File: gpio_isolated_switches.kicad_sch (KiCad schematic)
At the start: 34 parts, among them J2 Conn_01x02, J3 Conn_01x02, J4 Conn_01x02, J5 SBC GPIO, J6 Conn_01x02, J7 Conn_01x02, Q2 BUK7M10-40EX, Q3 BUK7M10-40EX, Q4 BUK7M10-40EX, U1 TLP291-4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

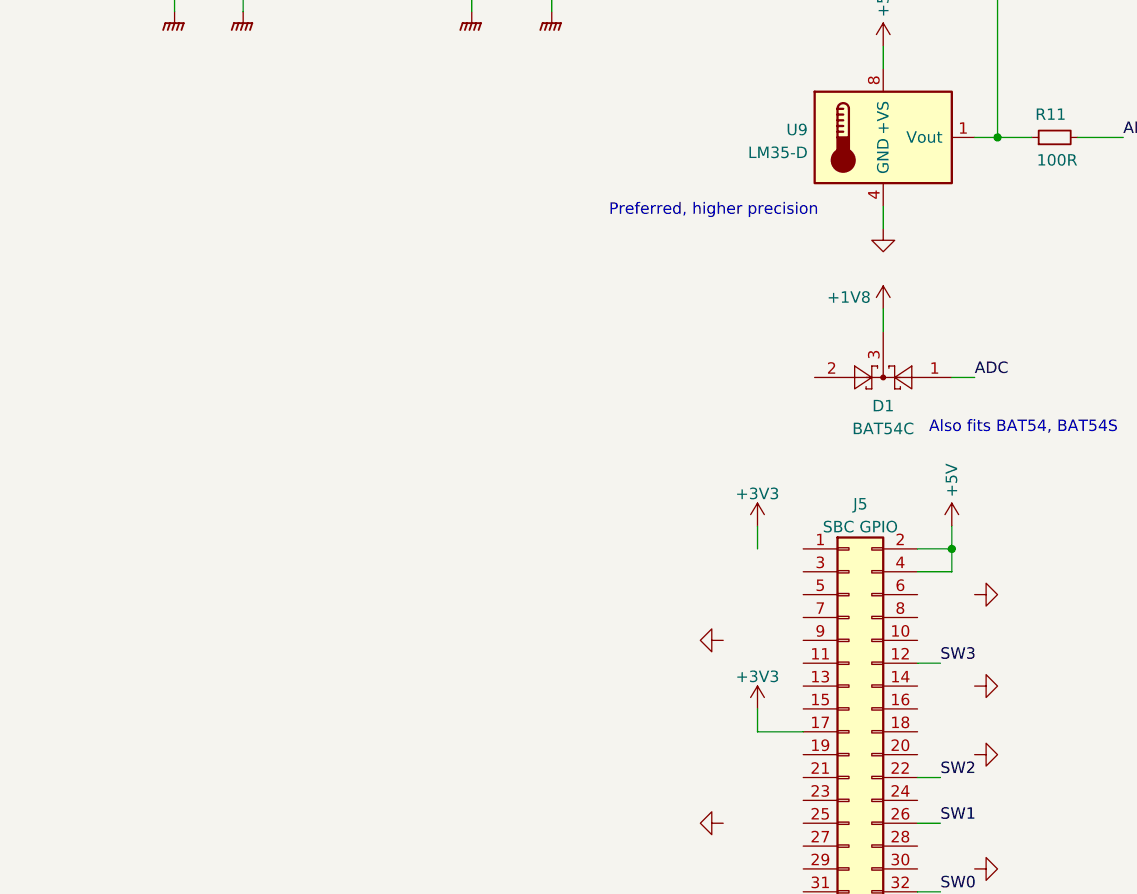
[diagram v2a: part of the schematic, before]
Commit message: Adding DS18B20 as an optional temperature sensor
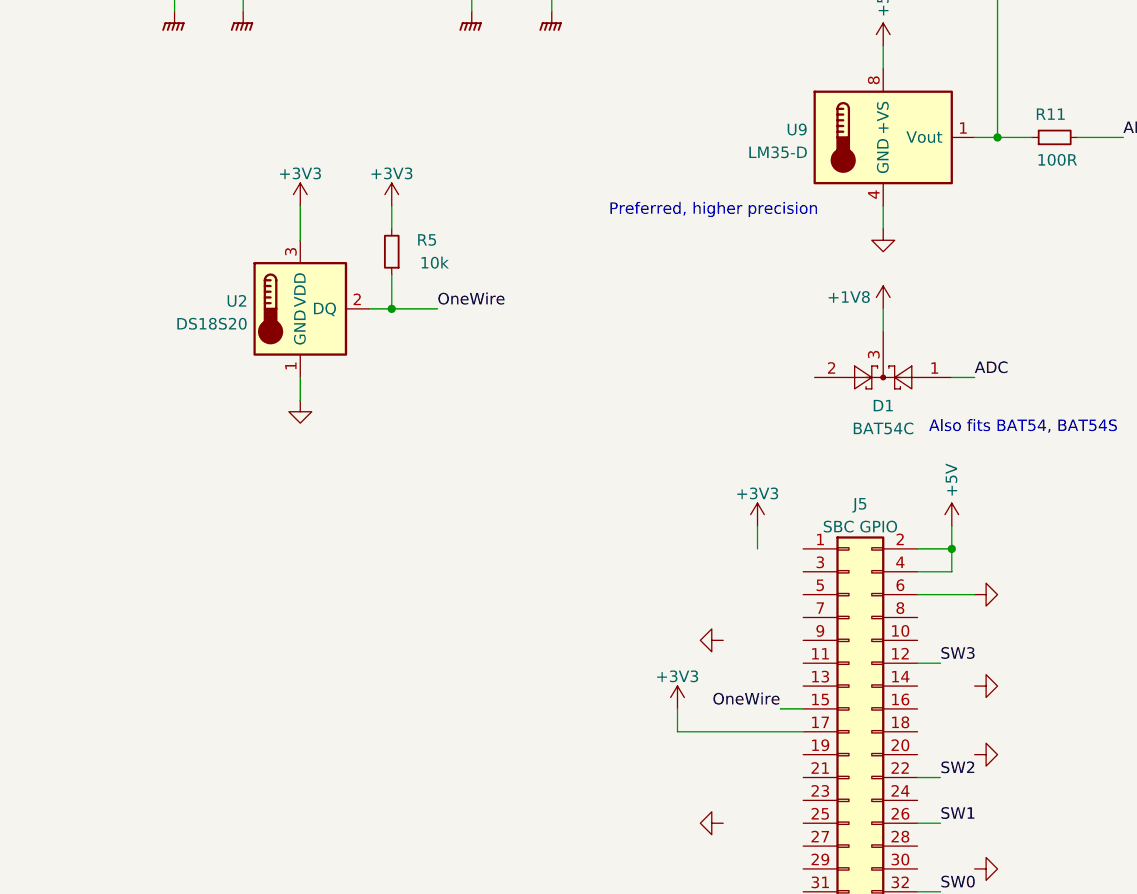
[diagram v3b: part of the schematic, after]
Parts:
- added R5: 10k, Resistor_SMD:R_0603_1608Metric, symbol Device:R_Small
- added U2: DS18S20, Package_TO_SOT_THT:TO-92_Inline, symbol Sensor_Temperature:DS18S20
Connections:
- net +3V3: now also R5.2, U2.3 (VDD)
- net GND: now also J5.6 (Pin_6), U2.1 (GND)
- net OneWire: now reaches J5.15 (Pin_15)
- net OneWire: now also R5.1, U2.2 (DQ)
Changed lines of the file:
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@@
   (junction (at 214.63 29.21) (diameter 0) (color 0 0 0 0)
   )
+  (junction (at 196.85 82.55) (diameter 0) (color 0 0 0 0)
+  )
   (junction (at 90.17 73.66) (diameter 0) (color 0 0 0 0)
   )
@@
     (stroke (width 0) (type default) (color 0 0 0 0))
   )
+  (wire (pts (xy 196.85 78.74) (xy 196.85 82.55))
+    (stroke (width 0) (type default) (color 0 0 0 0))
+  )
   (wire (pts (xy 255.27 154.94) (xy 269.24 154.94))
     (stroke (width 0) (type default) (color 0 0 0 0))
@@
     (stroke (width 0) (type default) (color 0 0 0 0))
   )
+  (wire (pts (xy 228.6 129.54) (xy 242.57 129.54))
+    (stroke (width 0) (type default) (color 0 0 0 0))
+  )
   (wire (pts (xy 255.27 109.22) (xy 259.08 109.22))
     (stroke (width 0) (type default) (color 0 0 0 0))
@@
     (stroke (width 0) (type default) (color 0 0 0 0))
   )
-  (wire (pts (xy 237.49 129.54) (xy 242.57 129.54))
-    (stroke (width 0) (type default) (color 0 0 0 0))
-  )
   (wire (pts (xy 170.18 29.21) (xy 180.34 29.21))
     (stroke (width 0) (type default) (color 0 0 0 0))
@@
     (stroke (width 0) (type default) (color 0 0 0 0))
   )
+  (wire (pts (xy 196.85 82.55) (xy 201.93 82.55))
+    (stroke (width 0) (type default) (color 0 0 0 0))
+  )
   (wire (pts (xy 170.18 31.75) (xy 172.72 31.75))
     (stroke (width 0) (type default) (color 0 0 0 0))
@@
     (stroke (width 0) (type default) (color 0 0 0 0))
   )
+  (wire (pts (xy 255.27 114.3) (xy 261.62 114.3))
+    (stroke (width 0) (type default) (color 0 0 0 0))
+  )
   (wire (pts (xy 58.42 39.37) (xy 73.66 39.37))
     (stroke (width 0) (type default) (color 0 0 0 0))
@@
     (stroke (width 0) (type default) (color 0 0 0 0))
   )
+  (wire (pts (xy 186.69 71.12) (xy 186.69 74.93))
+    (stroke (width 0) (type default) (color 0 0 0 0))
+  )
   (wire (pts (xy 101.6 162.56) (xy 101.6 161.29))
     (stroke (width 0) (type default) (color 0 0 0 0))
@@
     (stroke (width 0) (type default) (color 0 0 0 0))
   )
+  (wire (pts (xy 196.85 71.12) (xy 196.85 73.66))
+    (stroke (width 0) (type default) (color 0 0 0 0))
+  )
   (wire (pts (xy 255.27 147.32) (xy 257.81 147.32))
     (stroke (width 0) (type default) (color 0 0 0 0))
@@
     (stroke (width 0) (type default) (color 0 0 0 0))
   )
+  (wire (pts (xy 194.31 82.55) (xy 196.85 82.55))
+    (stroke (width 0) (type default) (color 0 0 0 0))
+  )
   (wire (pts (xy 58.42 34.29) (xy 73.66 34.29))
     (stroke (width 0) (type default) (color 0 0 0 0))
@@
     (stroke (width 0) (type default) (color 0 0 0 0))
   )
+  (wire (pts (xy 186.69 90.17) (xy 186.69 92.71))
+    (stroke (width 0) (type default) (color 0 0 0 0))
+  )
   (wire (pts (xy 273.05 24.13) (xy 273.05 22.86))
     (stroke (width 0) (type default) (color 0 0 0 0))
@@
     (stroke (width 0) (type default) (color 0 0 0 0))
   )
-  (wire (pts (xy 237.49 129.54) (xy 237.49 127))
+  (wire (pts (xy 228.6 129.54) (xy 228.6 127))
     (stroke (width 0) (type default) (color 0 0 0 0))
   )
@@
     (stroke (width 0) (type default) (color 0 0 0 0))
   )
+  (wire (pts (xy 240.03 127) (xy 242.57 127))
+    (stroke (width 0) (type default) (color 0 0 0 0))
+  )
   (wire (pts (xy 214.63 36.83) (xy 214.63 49.53))
     (stroke (width 0) (type default) (color 0 0 0 0))
@@
     (effects (font (size 1.27 1.27)) (justify left bottom))
   )
+  (label "OneWire" (at 201.93 82.55 0)
+    (effects (font (size 1.27 1.27)) (justify left bottom))
+  )
   (label "SW1" (at 27.94 86.36 180)
     (effects (font (size 1.27 1.27)) (justify right bottom))
   )
+  (label "OneWire" (at 240.03 127 180)
+    (effects (font (size 1.27 1.27)) (justify right bottom))
+  )
   (label "ADC" (at 278.13 63.5 0)
     (effects (font (size 1.27 1.27)) (justify left bottom))
@@
     (pin "1")
   )
-  (symbol (lib_id "power:+3V3") (at 237.49 127 0) (unit 1)
+  (symbol (lib_id "Sensor_Temperature:DS18S20") (at 186.69 82.55 0) (unit 1)
     (in_bom yes) (on_board yes) (fields_autoplaced)
-    (property "Reference" "#PWR012" (id 0) (at 237.49 130.81 0)
+    (property "Reference" "U2" (id 0) (at 180.8481 81.7153 0)
+      (effects (font (size 1.27 1.27)) (justify right))
+    )
+    (property "Value" "DS18S20" (id 1) (at 180.8481 84.2522 0)
+      (effects (font (size 1.27 1.27)) (justify right))
+    )
+    (property "Footprint" "Package_TO_SOT_THT:TO-92_Inline" (id 2) (at 161.29 88.9 0)
       (effects (font (size 1.27 1.27)) hide)
     )
-    (property "Value" "+3V3" (id 1) (at 237.49 123.4242 0))
-    (property "Footprint" "" (id 2) (at 237.49 127 0)
+    (property "Datasheet" "http://datasheets.maximintegrated.com/en/ds/DS18S20.pdf" (id 3) (at 182.88 76.2 0)
       (effects (font (size 1.27 1.27)) hide)
     )
-    (property "Datasheet" "" (id 3) (at 237.49 127 0)
+    (pin "1")
+    (pin "2")
+    (pin "3")
+  )
+  (symbol (lib_id "power:+3V3") (at 228.6 127 0) (unit 1)
+    (in_bom yes) (on_board yes) (fields_autoplaced)
+    (property "Reference" "#PWR012" (id 0) (at 228.6 130.81 0)
+      (effects (font (size 1.27 1.27)) hide)
+    )
+    (property "Value" "+3V3" (id 1) (at 228.6 123.4242 0))
+    (property "Footprint" "" (id 2) (at 228.6 127 0)
+      (effects (font (size 1.27 1.27)) hide)
+    )
+    (property "Datasheet" "" (id 3) (at 228.6 127 0)
       (effects (font (size 1.27 1.27)) hide)
     )
@@
     (pin "9")
   )
+  (symbol (lib_id "power:+3V3") (at 186.69 71.12 0) (unit 1)
+    (in_bom yes) (on_board yes) (fields_autoplaced)
+    (property "Reference" "#PWR0102" (id 0) (at 186.69 74.93 0)
+      (effects (font (size 1.27 1.27)) hide)
+    )
+    (property "Value" "+3V3" (id 1) (at 186.69 67.5442 0))
+    (property "Footprint" "" (id 2) (at 186.69 71.12 0)
+      (effects (font (size 1.27 1.27)) hide)
+    )
+    (property "Datasheet" "" (id 3) (at 186.69 71.12 0)
+      (effects (font (size 1.27 1.27)) hide)
+    )
+    (pin "1")
+  )
   (symbol (lib_id "Device:R_Small") (at 33.02 86.36 90) (unit 1)
     (in_bom yes) (on_board yes)
@@
     (pin "1")
   )
+  (symbol (lib_id "power:GND") (at 186.69 92.71 0) (unit 1)
+    (in_bom yes) (on_board yes)
+    (property "Reference" "#PWR0104" (id 0) (at 186.69 99.06 0)
+      (effects (font (size 1.27 1.27)) hide)
+    )
+    (property "Value" "GND" (id 1) (at 186.817 97.1042 0)
+      (effects (font (size 1.27 1.27)) hide)
+    )
+    (property "Footprint" "" (id 2) (at 186.69 92.71 0)
+      (effects (font (size 1.27 1.27)) hide)
+    )
+    (property "Datasheet" "" (id 3) (at 186.69 92.71 0)
+      (effects (font (size 1.27 1.27)) hide)
+    )
+    (pin "1")
+  )
   (symbol (lib_id "power:GNDPWR") (at 172.72 49.53 0) (unit 1)
     (in_bom yes) (on_board yes) (fields_autoplaced)
@@
     (pin "1")
   )
+  (symbol (lib_id "Device:R_Small") (at 196.85 76.2 180) (unit 1)
+    (in_bom yes) (on_board yes)
+    (property "Reference" "R5" (id 0) (at 201.93 74.93 0)
+      (effects (font (size 1.27 1.27)) (justify left))
+    )
+    (property "Value" "10k" (id 1) (at 203.2 77.47 0)
+      (effects (font (size 1.27 1.27)) (justify left))
+    )
+    (property "Footprint" "Resistor_SMD:R_0603_1608Metric" (id 2) (at 196.85 76.2 0)
+      (effects (font (size 1.27 1.27)) hide)
+    )
+    (property "Datasheet" "~" (id 3) (at 196.85 76.2 0)
+      (effects (font (size 1.27 1.27)) hide)
+    )
+    (pin "1")
+    (pin "2")
+  )
   (symbol (lib_id "Isolator:TLP291-4") (at 50.8 128.27 0) (unit 3)
     (in_bom yes) (on_board yes)
@@
     (pin "2")
   )
+  (symbol (lib_id "power:+3V3") (at 196.85 71.12 0) (unit 1)
+    (in_bom yes) (on_board yes) (fields_autoplaced)
+    (property "Reference" "#PWR0101" (id 0) (at 196.85 74.93 0)
+      (effects (font (size 1.27 1.27)) hide)
+    )
+    (property "Value" "+3V3" (id 1) (at 196.85 67.5442 0))
+    (property "Footprint" "" (id 2) (at 196.85 71.12 0)
+      (effects (font (size 1.27 1.27)) hide)
+    )
+    (property "Datasheet" "" (id 3) (at 196.85 71.12 0)
+      (effects (font (size 1.27 1.27)) hide)
+    )
+    (pin "1")
+  )
   (symbol (lib_id "Connector_Generic:Conn_01x02") (at 165.1 29.21 0) (mirror y) (unit 1)
     (in_bom yes) (on_board yes)
@@
       (reference "#PWR017") (unit 1) (value "GND") (footprint "")
     )
+    (path "/c6dfda58-11ef-4f53-bf32-136eb23170da"
+      (reference "#PWR0101") (unit 1) (value "+3V3") (footprint "")
+    )
+    (path "/4663fb69-4d9b-4727-b995-87b7acc7cb95"
+      (reference "#PWR0102") (unit 1) (value "+3V3") (footprint "")
+    )
     (path "/a69eddcb-91e5-4a4d-871a-916279d9cc17"
       (reference "#PWR0103") (unit 1) (value "+1V8") (footprint "")
     )
+    (path "/88ba13da-1702-4c6c-8487-9d3b9bc51e02"
+      (reference "#PWR0104") (unit 1) (value "GND") (footprint "")
+    )
     (path "/0ce7e08c-2867-45a8-909b-38a701beb917"
       (reference "#PWR0105") (unit 1) (value "+5V") (footprint "")
@@
       (reference "R4") (unit 1) (value "1k") (footprint "Resistor_SMD:R_0603_1608Metric")
     )
+    (path "/9b899abc-281b-41d0-a91a-7e95d51a12d4"
+      (reference "R5") (unit 1) (value "10k") (footprint "Resistor_SMD:R_0603_1608Metric")
+    )
     (path "/10fa49e4-90da-4ade-8808-48ab8619ef12"
       (reference "R6") (unit 1) (value "10k") (footprint "Resistor_SMD:R_0603_1608Metric")
@@
       (reference "U1") (unit 4) (value "TLP291-4") (footprint "Package_SO:SOIC-16_4.55x10.3mm_P1.27mm")
     )
+    (path "/29988e38-c0ed-44d5-9a95-db1388cb37b3"
+      (reference "U2") (unit 1) (value "DS18S20") (footprint "Package_TO_SOT_THT:TO-92_Inline")
+    )
     (path "/0079e046-7c9d-4bdb-8308-0d0aa638e160"
